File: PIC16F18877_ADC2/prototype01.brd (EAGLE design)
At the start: 95 x 72 mm, 39 parts, among them CN1 12V_IN, CN10 PIC_PORTD_IF, CN2 PIC_PORTA_IF, CN3 UART_IF, CN4 PIC_CN_H, CN5 AE-MICRO-SD-DIP, CN6 I2C_IF, CN7 PIC_PORTB_IF, CN8 PIC_PORTE_IF, CN9 PIC_PORTC_IF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

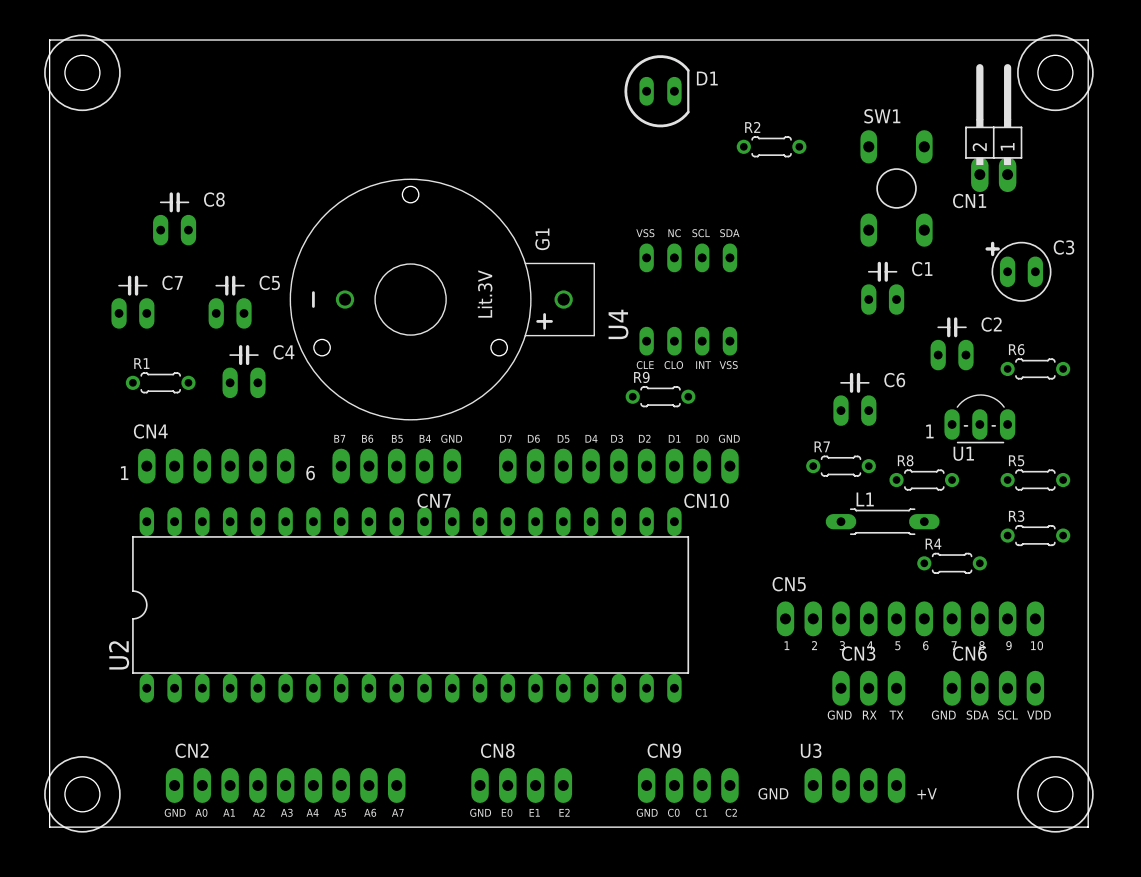
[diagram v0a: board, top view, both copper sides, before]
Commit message: 部品配置を修正
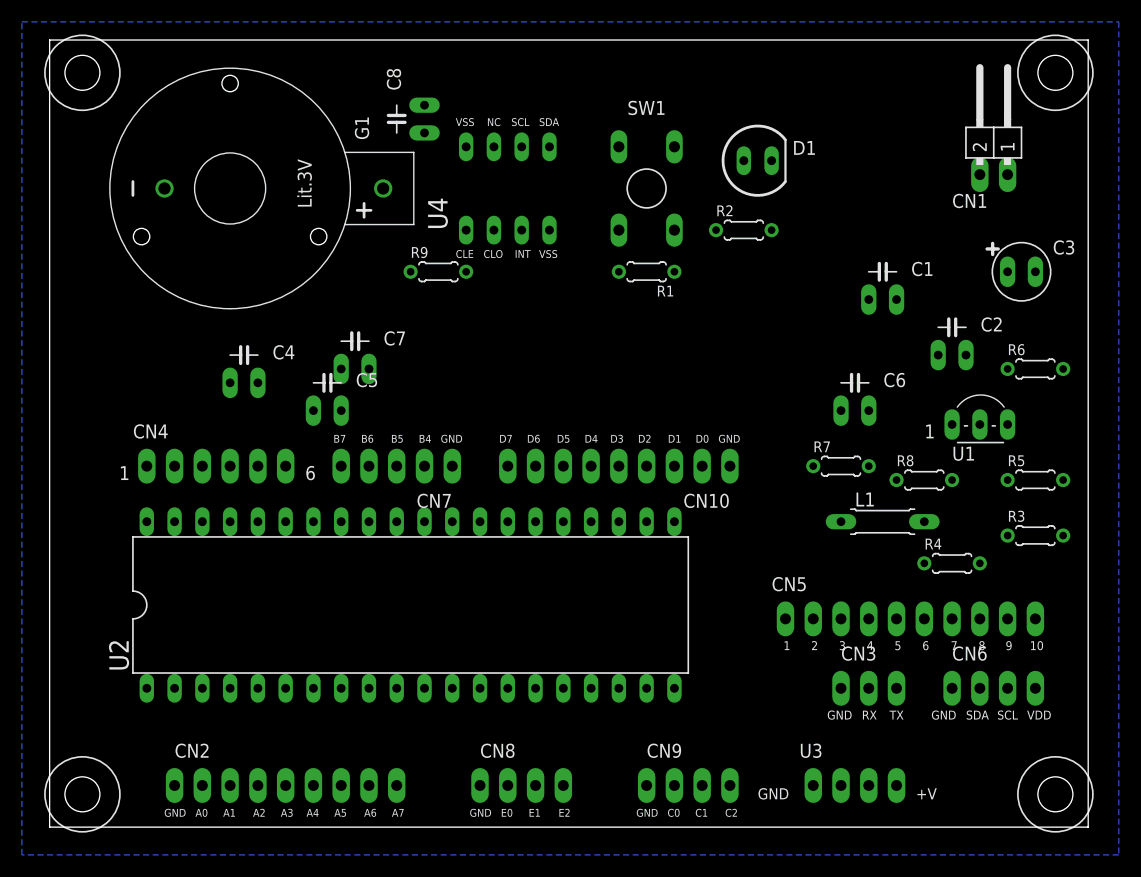
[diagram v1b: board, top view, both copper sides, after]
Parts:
- moved R1 45.6 mm to (54.6, 50.8), turned to 180 degrees
- moved C8 25.0 mm to (34.3, 64.8), turned to 90 degrees
- moved R9 23.3 mm to (35.6, 50.8)
- moved C7 20.9 mm to (27.9, 41.9)
- moved G1 19.4 mm to (16.5, 58.4)
- moved U4 19.4 mm to (38.1, 54.6)
- moved SW1 19.3 mm to (57.1, 54.6), turned to 180 degrees
- moved C5 12.6 mm to (25.4, 38.1)
- moved D1 10.9 mm to (64.8, 61.0)
- moved R2 8.03 mm to (63.5, 54.6)
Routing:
- added copper zone on layer 16, net 0V

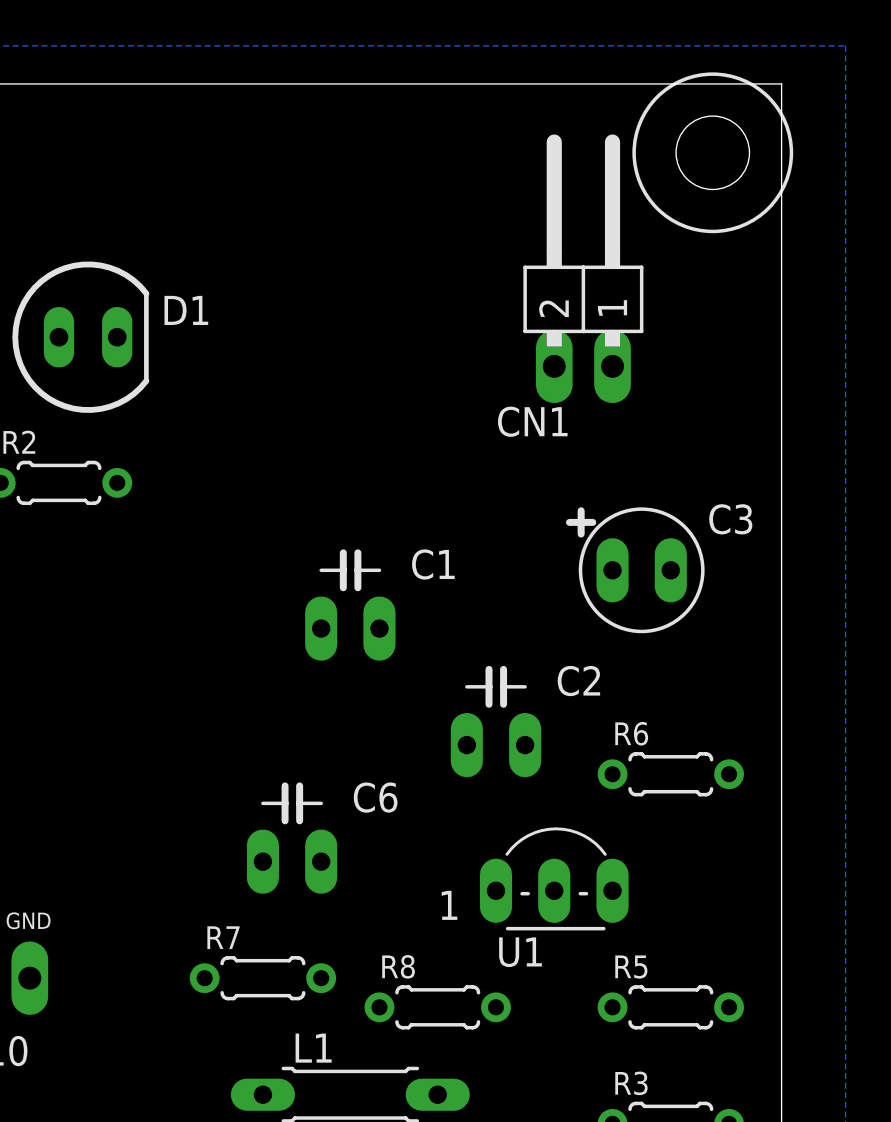
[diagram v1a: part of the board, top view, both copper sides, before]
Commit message: 部品配置を修正
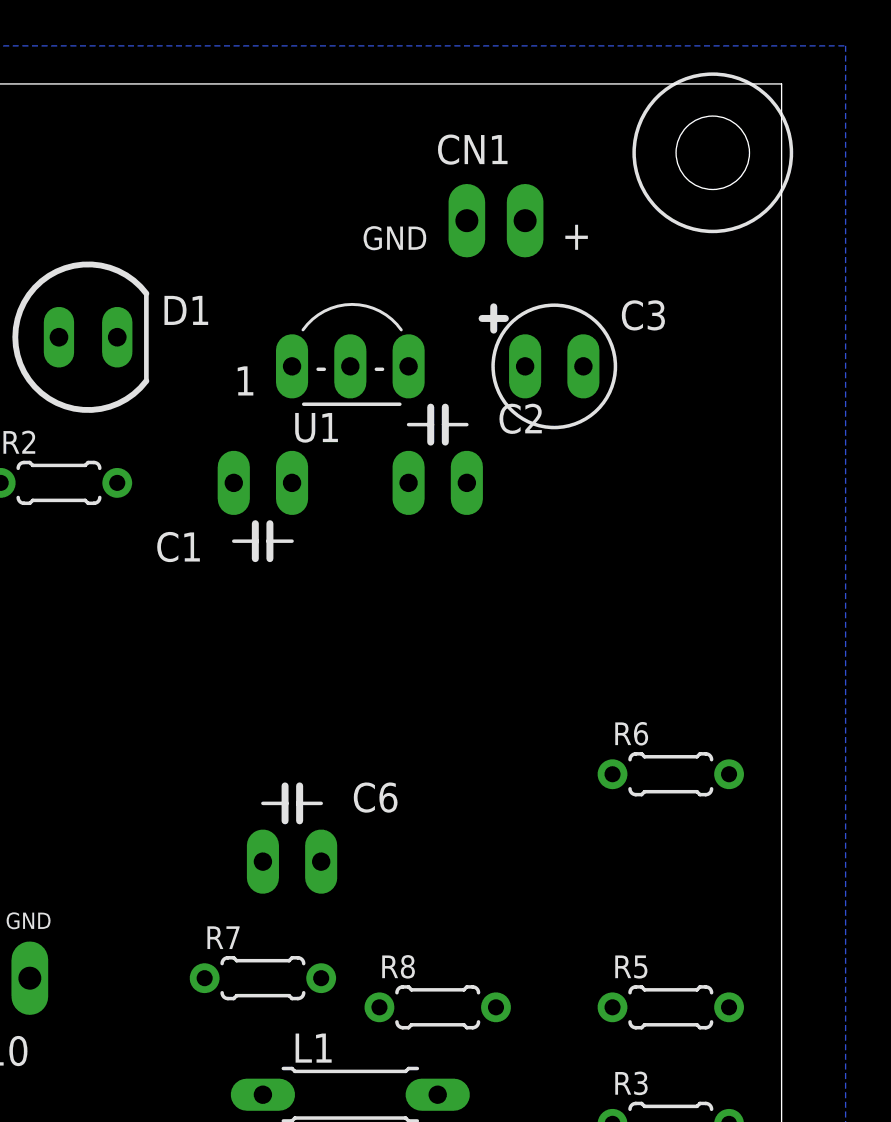
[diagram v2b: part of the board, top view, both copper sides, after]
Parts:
- CN1: device Connectors:HEADER_L_2PIN -> PartsForProto:HEADER_2PIN_POWER_IF
- moved U1 24.5 mm to (73.7, 59.7)
- moved C2 11.7 mm to (80.0, 54.6)
- moved C3 9.67 mm to (85.1, 59.7)
- moved C1 7.41 mm to (72.4, 54.6), turned to 180 degrees
- moved CN1 7.18 mm to (81.3, 66.0)
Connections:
- net +12V: now also CN1.2; no longer CN1.1
- net 0V: now also CN1.1; no longer CN1.2
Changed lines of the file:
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@@
 </autorouter>
 <elements>
-<element name="C1" library="Parts" package="CAP_100MIL" value="1uF" x="76.2" y="48.26"/>
-<element name="C2" library="Parts" package="CAP_100MIL" value="1uF" x="82.55" y="43.18"/>
-<element name="C3" library="Parts" package="ELECAP_D5_100MIL" value="10uF" x="88.9" y="50.8"/>
+<element name="C1" library="Parts" package="CAP_100MIL" value="1uF" x="72.39" y="54.61" rot="R180"/>
+<element name="C2" library="Parts" package="CAP_100MIL" value="1uF" x="80.01" y="54.61"/>
+<element name="C3" library="Parts" package="ELECAP_D5_100MIL" value="10uF" x="85.09" y="59.69"/>
 <element name="C4" library="Parts" package="CAP_100MIL" value="0.1uF" x="17.78" y="40.64"/>
 <element name="C5" library="Parts" package="CAP_100MIL" value="0.1uF" x="25.4" y="38.1"/>
@@
 <element name="C7" library="Parts" package="CAP_100MIL" value="0.1uF" x="27.94" y="41.91"/>
 <element name="C8" library="Parts" package="CAP_100MIL" value="0.1uF" x="34.29" y="64.77" rot="R90"/>
-<element name="CN1" library="Connectors" package="HEADER_L_2PIN" value="12V_IN" x="86.36" y="60.96"/>
+<element name="CN1" library="PartsForProto" package="HEADER_2PIN_POWER_IF" value="12V_IN" x="81.28" y="66.04"/>
 <element name="CN10" library="PartsForProto" package="PIC_PORTD_IF_9PIN" value="PIC_PORTD_IF" x="62.23" y="33.02" rot="R180"/>
 <element name="CN2" library="PartsForProto" package="PIC_PORTA_IF_9PIN" value="PIC_PORTA_IF" x="11.43" y="3.81"/>
@@
 <attribute name="VALUE" x="57.658" y="65.532" size="1.27" layer="27" ratio="10" rot="R180"/>
 </element>
-<element name="U1" library="Parts" package="TO92-LINE" value="XC6202P332TH" x="82.55" y="36.83"/>
+<element name="U1" library="Parts" package="TO92-LINE" value="XC6202P332TH" x="73.66" y="59.69"/>
 <element name="U2" library="Parts" package="DIL40" value="PIC16F18877-I/P" x="33.02" y="20.32"/>
 <element name="U3" library="PartsForProto" package="AE-AQM1602A" value="AE-AQM1602A" x="69.85" y="3.81"/>
@@
 <contactref element="C1" pad="2"/>
 <contactref element="C2" pad="2"/>
-<contactref element="CN1" pad="2"/>
+<contactref element="CN1" pad="1"/>
 <contactref element="C3" pad="-"/>
 <contactref element="R9" pad="1"/>
@@
 <contactref element="U1" pad="1"/>
 <contactref element="CN6" pad="4"/>
-<wire x1="82.55" y1="36.83" x2="74.93" y2="48.26" width="0" layer="19" extent="1-1"/>
-<wire x1="82.55" y1="31.75" x2="82.55" y2="36.83" width="0" layer="19" extent="1-1"/>
-<wire x1="80.01" y1="27.94" x2="82.55" y2="31.75" width="0" layer="19" extent="1-1"/>
-<wire x1="74.93" y1="33.02" x2="80.01" y2="27.94" width="0" layer="19" extent="1-1"/>
+<wire x1="73.66" y1="54.61" x2="73.66" y2="59.69" width="0" layer="19" extent="1-1"/>
+<wire x1="74.93" y1="33.02" x2="73.66" y2="54.61" width="0" layer="19" extent="1-1"/>
+<wire x1="80.01" y1="27.94" x2="74.93" y2="33.02" width="0" layer="19" extent="1-1"/>
+<wire x1="82.55" y1="31.75" x2="80.01" y2="27.94" width="0" layer="19" extent="1-1"/>
 <wire x1="90.17" y1="12.7" x2="80.01" y2="27.94" width="0" layer="19" extent="1-1"/>
 <wire x1="77.47" y1="3.81" x2="90.17" y2="12.7" width="0" layer="19" extent="1-1"/>
-<wire x1="52.07" y1="50.8" x2="74.93" y2="48.26" width="0" layer="19" extent="1-1"/>
+<wire x1="52.07" y1="50.8" x2="73.66" y2="54.61" width="0" layer="19" extent="1-1"/>
 <wire x1="24.13" y1="38.1" x2="52.07" y2="50.8" width="0" layer="19" extent="1-1"/>
 <wire x1="16.51" y1="40.64" x2="24.13" y2="38.1" width="0" layer="19" extent="1-1"/>
@@
 <contactref element="C2" pad="1"/>
 <contactref element="U1" pad="3"/>
-<contactref element="CN1" pad="1"/>
+<contactref element="CN1" pad="2"/>
 <contactref element="C3" pad="+"/>
-<wire x1="87.63" y1="50.8" x2="87.63" y2="59.69" width="0" layer="19" extent="1-1"/>
-<wire x1="81.28" y1="43.18" x2="87.63" y2="50.8" width="0" layer="19" extent="1-1"/>
-<wire x1="87.63" y1="36.83" x2="81.28" y2="43.18" width="0" layer="19" extent="1-1"/>
+<wire x1="83.82" y1="59.69" x2="83.82" y2="66.04" width="0" layer="19" extent="1-1"/>
+<wire x1="78.74" y1="59.69" x2="83.82" y2="59.69" width="0" layer="19" extent="1-1"/>
+<wire x1="78.74" y1="54.61" x2="78.74" y2="59.69" width="0" layer="19" extent="1-1"/>
 </signal>
 <signal name="N$16">

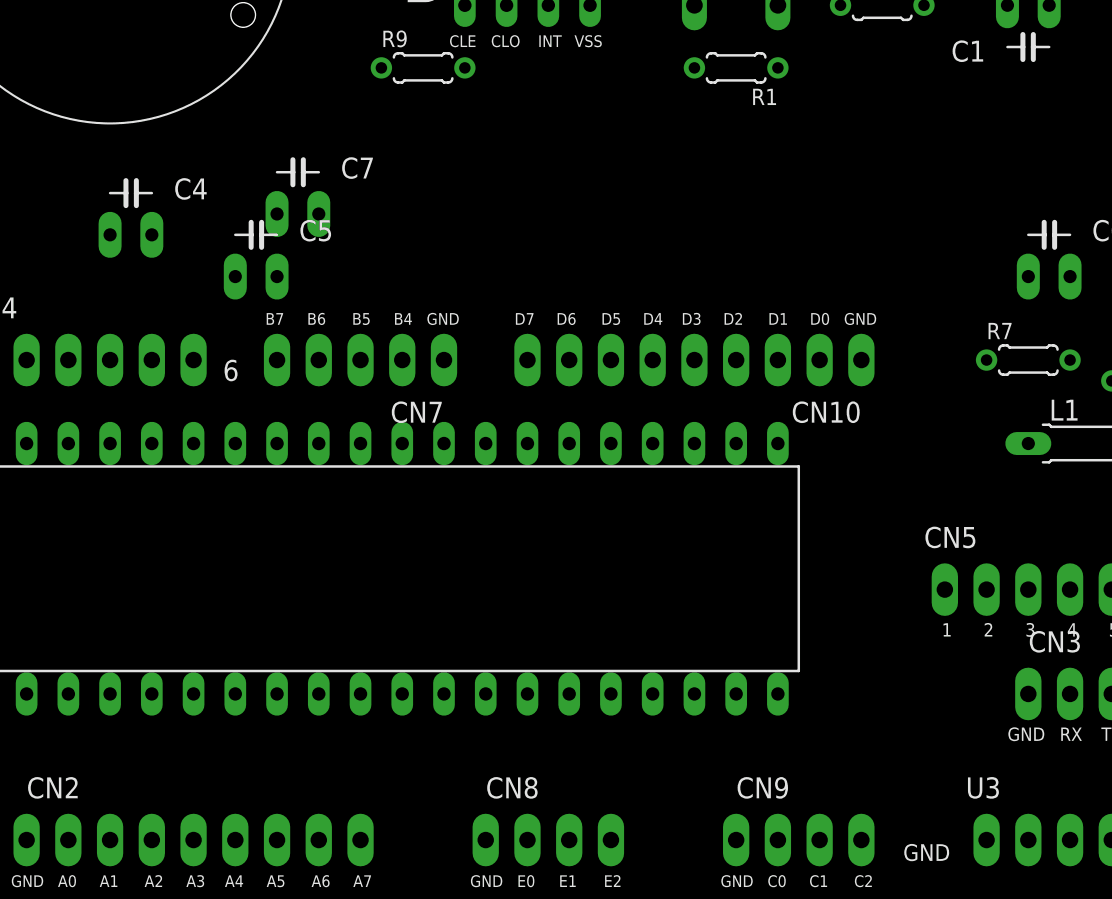
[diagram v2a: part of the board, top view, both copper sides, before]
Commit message: 部品配置を修正
パスコン
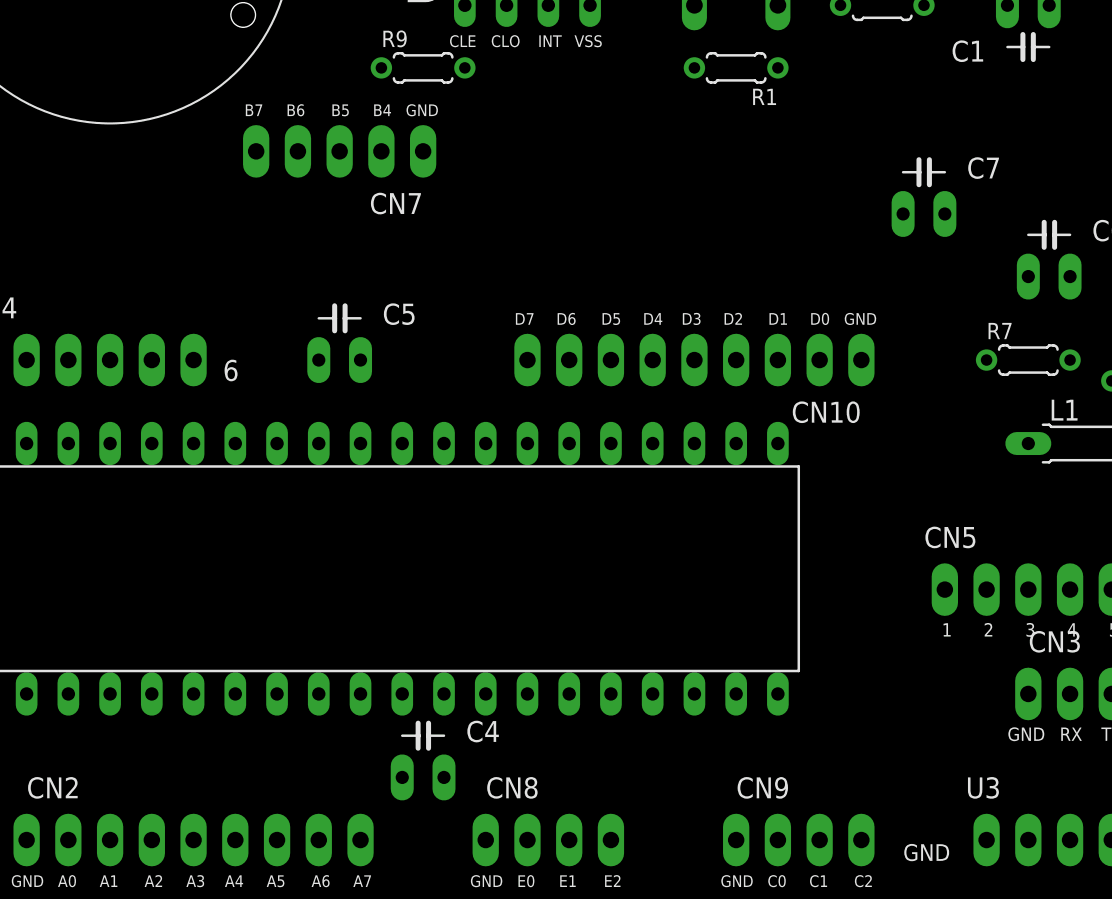
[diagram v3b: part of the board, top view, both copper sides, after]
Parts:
- moved C7 38.1 mm to (66.0, 41.9)
- moved C4 37.5 mm to (35.6, 7.62)
- moved CN7 12.8 mm to (35.6, 45.7)
- moved C5 7.18 mm to (30.5, 33.0)
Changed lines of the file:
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@@
 <element name="C2" library="Parts" package="CAP_100MIL" value="1uF" x="80.01" y="54.61"/>
 <element name="C3" library="Parts" package="ELECAP_D5_100MIL" value="10uF" x="85.09" y="59.69"/>
-<element name="C4" library="Parts" package="CAP_100MIL" value="0.1uF" x="17.78" y="40.64"/>
-<element name="C5" library="Parts" package="CAP_100MIL" value="0.1uF" x="25.4" y="38.1"/>
+<element name="C4" library="Parts" package="CAP_100MIL" value="0.1uF" x="35.56" y="7.62"/>
+<element name="C5" library="Parts" package="CAP_100MIL" value="0.1uF" x="30.48" y="33.02"/>
 <element name="C6" library="Parts" package="CAP_100MIL" value="10uF" x="73.66" y="38.1"/>
-<element name="C7" library="Parts" package="CAP_100MIL" value="0.1uF" x="27.94" y="41.91"/>
+<element name="C7" library="Parts" package="CAP_100MIL" value="0.1uF" x="66.04" y="41.91"/>
 <element name="C8" library="Parts" package="CAP_100MIL" value="0.1uF" x="34.29" y="64.77" rot="R90"/>
 <element name="CN1" library="PartsForProto" package="HEADER_2PIN_POWER_IF" value="12V_IN" x="81.28" y="66.04"/>
@@
 <element name="CN5" library="PartsForProto" package="AE-MICRO-SD-DIP" value="AE-MICRO-SD-DIP" x="67.31" y="19.05"/>
 <element name="CN6" library="PartsForProto" package="I2C_IF_4PIN" value="I2C_IF" x="82.55" y="12.7"/>
-<element name="CN7" library="PartsForProto" package="PIC_PORTB_IF_5PIN" value="PIC_PORTB_IF" x="36.83" y="33.02" rot="R180"/>
+<element name="CN7" library="PartsForProto" package="PIC_PORTB_IF_5PIN" value="PIC_PORTB_IF" x="35.56" y="45.72" rot="R180"/>
 <element name="CN8" library="PartsForProto" package="PIC_PORTE_IF_4PIN" value="PIC_PORTE_IF" x="39.37" y="3.81"/>
 <element name="CN9" library="PartsForProto" package="PIC_PORTC_IF_4PIN" value="PIC_PORTC_IF" x="54.61" y="3.81"/>
@@
 <contactref element="CN4" pad="4"/>
 <contactref element="CN7" pad="5"/>
-<wire x1="16.51" y1="33.02" x2="26.67" y2="33.02" width="0" layer="19" extent="1-1"/>
+<wire x1="16.51" y1="33.02" x2="25.4" y2="45.72" width="0" layer="19" extent="1-1"/>
 <wire x1="8.89" y1="27.94" x2="16.51" y2="33.02" width="0" layer="19" extent="1-1"/>
 </signal>
@@
 <contactref element="U2" pad="39"/>
 <contactref element="CN7" pad="4"/>
-<wire x1="19.05" y1="33.02" x2="29.21" y2="33.02" width="0" layer="19" extent="1-1"/>
+<wire x1="19.05" y1="33.02" x2="27.94" y2="45.72" width="0" layer="19" extent="1-1"/>
 <wire x1="11.43" y1="27.94" x2="19.05" y2="33.02" width="0" layer="19" extent="1-1"/>
 </signal>
@@
 <wire x1="72.39" y1="27.94" x2="74.93" y2="19.05" width="0" layer="19" extent="1-1"/>
 <wire x1="72.39" y1="38.1" x2="72.39" y2="27.94" width="0" layer="19" extent="1-1"/>
-<wire x1="26.67" y1="41.91" x2="72.39" y2="38.1" width="0" layer="19" extent="1-1"/>
+<wire x1="64.77" y1="41.91" x2="72.39" y2="38.1" width="0" layer="19" extent="1-1"/>
 </signal>
 <signal name="N$12">
@@
 <wire x1="77.47" y1="3.81" x2="90.17" y2="12.7" width="0" layer="19" extent="1-1"/>
 <wire x1="52.07" y1="50.8" x2="73.66" y2="54.61" width="0" layer="19" extent="1-1"/>
-<wire x1="24.13" y1="38.1" x2="52.07" y2="50.8" width="0" layer="19" extent="1-1"/>
-<wire x1="16.51" y1="40.64" x2="24.13" y2="38.1" width="0" layer="19" extent="1-1"/>
-<wire x1="11.43" y1="33.02" x2="16.51" y2="40.64" width="0" layer="19" extent="1-1"/>
-<wire x1="29.21" y1="27.94" x2="24.13" y2="38.1" width="0" layer="19" extent="1-1"/>
+<wire x1="29.21" y1="33.02" x2="52.07" y2="50.8" width="0" layer="19" extent="1-1"/>
+<wire x1="29.21" y1="27.94" x2="29.21" y2="33.02" width="0" layer="19" extent="1-1"/>
 <wire x1="34.29" y1="12.7" x2="29.21" y2="27.94" width="0" layer="19" extent="1-1"/>
+<wire x1="34.29" y1="7.62" x2="34.29" y2="12.7" width="0" layer="19" extent="1-1"/>
+<wire x1="11.43" y1="33.02" x2="29.21" y2="33.02" width="0" layer="19" extent="1-1"/>
 </signal>
 <signal name="+12V">
@@
 <contactref element="CN7" pad="2"/>
 <contactref element="U2" pad="37"/>
-<wire x1="16.51" y1="27.94" x2="34.29" y2="33.02" width="0" layer="19" extent="1-1"/>
+<wire x1="16.51" y1="27.94" x2="33.02" y2="45.72" width="0" layer="19" extent="1-1"/>
 </signal>
 <signal name="N$19">
 <contactref element="U2" pad="38"/>
 <contactref element="CN7" pad="3"/>
-<wire x1="13.97" y1="27.94" x2="31.75" y2="33.02" width="0" layer="19" extent="1-1"/>
+<wire x1="13.97" y1="27.94" x2="30.48" y2="45.72" width="0" layer="19" extent="1-1"/>
 </signal>
 <signal name="RC0">
